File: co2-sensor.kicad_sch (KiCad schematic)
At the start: 51 parts, among them J1 Waveshare E-Ink, J2 USB-C Receptacle, J3 JST 2-PH, Q2 AO3400A, Q3 DMP2045U, SW1 SW_Push, SW2 SW_Push, SW3 SW_Push, SW4 SW_Push, SW5 SW_Push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

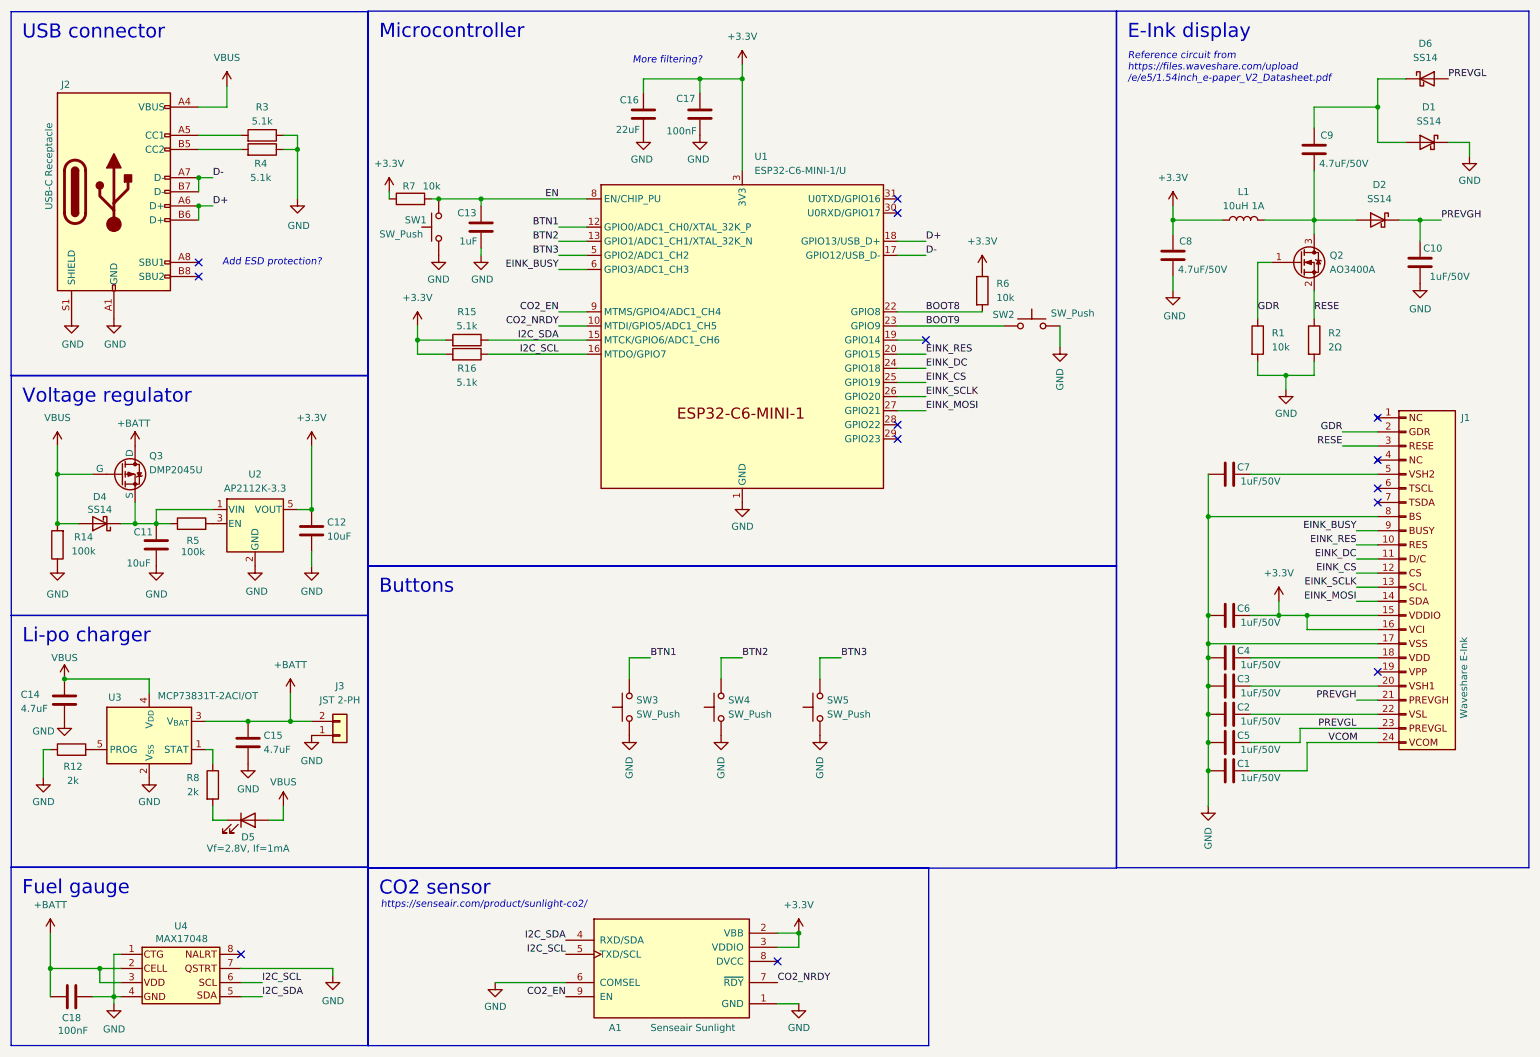
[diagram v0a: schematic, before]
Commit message: Add all LCSC part numbers
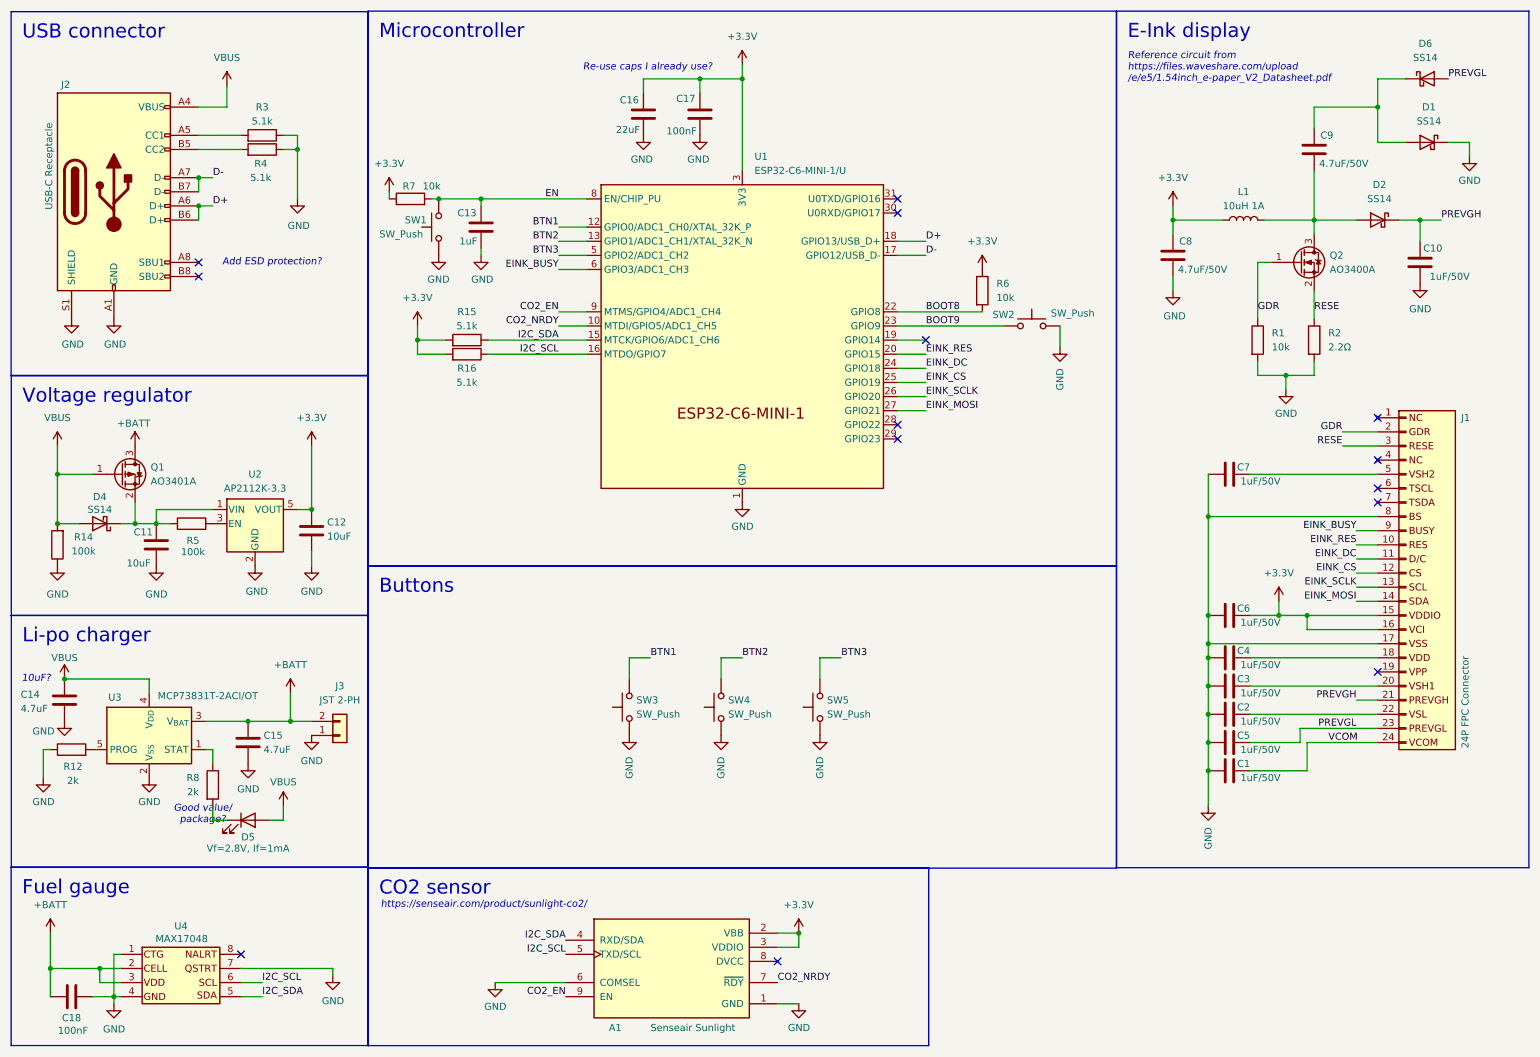
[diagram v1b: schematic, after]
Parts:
- removed Q3: DMP2045U, Package_TO_SOT_SMD:SOT-23, symbol Simulation_SPICE:PMOS
- added Q1: AO3401A, Package_TO_SOT_SMD:SOT-23, symbol Transistor_FET:AO3401A
- A1: now left out of the parts list
- C1, C10, C13, C2, C3, C4, C5, C6, C7: footprint Capacitor_SMD:C_0805_2012Metric -> Capacitor_SMD:C_0603_1608Metric; LCSC Part (none) -> C15849
- C11, C12: footprint Capacitor_SMD:C_0805_2012Metric -> Capacitor_SMD:C_0603_1608Metric; LCSC Part (none) -> C96446
- C14, C15, C8, C9: footprint Capacitor_SMD:C_0805_2012Metric -> Capacitor_SMD:C_1206_3216Metric; LCSC Part (none) -> C29823
- C16: LCSC Part (none) -> C45783
- C17, C18: LCSC Part (none) -> C1710
- D1, D2, D6: LCSC Part (none) -> C2480
- D4: footprint Diode_SMD:D_SOD-123 -> Diode_SMD:D_SMA; LCSC Part (none) -> C2480
- D5: LCSC Part (none) -> C2290
- J1: value Waveshare E-Ink -> 24P FPC Connector; footprint Connector_FFC-FPC:TE_2-1734839-4_1x24-1MP_P0.5mm_Horizontal -> Connector_FFC-FPC:Jushuo_AFC07-S24FCA-00_1x24-1MP_P0.50_Horizontal; LCSC Part (none) -> C262567
- J2: LCSC Part (none) -> C2988369
- J3: LCSC Part (none) -> C7433648
- L1: footprint Inductor_SMD:L_Ferrocore_DLG-0403 -> Inductor_SMD:L_1008_2520Metric; LCSC Part (none) -> C602018
- Q2: LCSC Part (none) -> C20917
- R1: LCSC Part (none) -> C25804
- R12, R8: footprint Capacitor_SMD:C_0805_2012Metric -> Resistor_SMD:R_0402_1005Metric; LCSC Part (none) -> C4109
- R14, R5: footprint Capacitor_SMD:C_0805_2012Metric -> Resistor_SMD:R_0402_1005Metric; LCSC Part (none) -> C25741
- R15, R16, R3, R4: footprint Capacitor_SMD:C_0805_2012Metric -> Resistor_SMD:R_0603_1608Metric; LCSC Part (none) -> C23186
- R2: value 2Ω -> 2.2Ω; LCSC Part (none) -> C22939
- R6, R7: footprint Capacitor_SMD:C_0805_2012Metric -> Resistor_SMD:R_0603_1608Metric; LCSC Part (none) -> C25804
- SW1, SW2, SW3, SW4, SW5: footprint Button_Switch_SMD:SW_SPST_SKQG_WithStem -> Button_Switch_SMD:SW_Push_1P1T_XKB_TS-1187A; LCSC Part (none) -> C318884
- U1: LCSC Part (none) -> C5736265
- U2: LCSC Part (none) -> C51118
- U3: LCSC Part (none) -> C424093
- U4: LCSC Part (none) -> C2682616
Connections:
- net +BATT: now also Q1.3 (D)
- net VBUS: now also Q1.1 (G)
- net at C11.1, D4.1 (K), R5.1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: now also Q1.2 (S)
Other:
- note added: "10uF?"
- note added: "Good value/ package?"
- note added: "Re-use caps I already use?"
- note removed: "More filtering?"

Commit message: Move components around
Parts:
- D1, D2, D4, D6: footprint Diode_SMD:D_SMA -> Diode_SMD:D_SOD-123; LCSC Part C2480 -> C8598
- J1: value 24P FPC Connector -> 24-pin FPC Connector; JLCPCB Position Offset (none) -> 0,0.381
- J2: JLCPCB Position Offset (none) -> 0,1.3335
- J3: JLCPCB Rotation Offset (none) -> 180
- U1: JLCPCB Position Offset (none) -> 0,-2.667
- U2, U3: JLCPCB Rotation Offset (none) -> 90
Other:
- note added: "Re-use caps sizes already use?"
- note removed: "10uF?"
- note removed: "Good value/ package?"
- note removed: "Re-use caps I already use?"
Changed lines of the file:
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@@
 	(title_block
 		(title "Low-Power CO2 Sensor")
-		(date "2024-11-01")
+		(date "2024-11-21")
 		(company "blinry <mail@blinry.org>")
 	)
@@
 		)
 	)
-	(text "Re-use caps I already use?"
+	(text "Re-use caps sizes already use?"
 		(exclude_from_sim no)
 		(at 126.492 22.098 0)
@@
 		)
 	)
-	(text "10uF?"
-		(exclude_from_sim no)
-		(at 16.51 132.08 0)
-		(effects
-			(font
-				(size 1.27 1.27)
-				(italic yes)
-				(color 255 0 0 1)
-			)
-		)
-	)
 	(text "Reference circuit from\nhttps://files.waveshare.com/upload\n/e/e5/1.54inch_e-paper_V2_Datasheet.pdf"
 		(exclude_from_sim no)
@@
 		)
 	)
-	(text "Good value/\npackage?"
-		(exclude_from_sim no)
-		(at 46.482 156.464 0)
-		(effects
-			(font
-				(size 1.27 1.27)
-				(italic yes)
-				(color 255 0 0 1)
-			)
-		)
-	)
 	(label "BTN2"
 		(at 143.51 128.27 0)
@@
 			)
 		)
-		(property "Footprint" "Diode_SMD:D_SMA"
+		(property "Footprint" "Diode_SMD:D_SOD-123"
 			(at 27.94 99.695 0)
 			(effects
@@
 			)
 		)
-		(property "LCSC Part" "C2480"
+		(property "LCSC Part" "C8598"
 			(at 27.94 104.14 0)
 			(effects
@@
 			)
 		)
+		(property "JLCPCB Position Offset" "0,-2.667"
+			(at 143.51 73.66 0)
+			(effects
+				(font
+					(size 1.27 1.27)
+				)
+				(hide yes)
+			)
+		)
 		(pin "46"
 		)
@@
 			)
 		)
+		(property "JLCPCB Rotation Offset" "180"
+			(at 71.12 142.24 0)
+			(effects
+				(font
+					(size 1.27 1.27)
+				)
+				(hide yes)
+			)
+		)
 		(pin "1"
 		)
@@
 			)
 		)
+		(property "JLCPCB Position Offset" "0,1.3335"
+			(at 30.48 44.45 0)
+			(effects
+				(font
+					(size 1.27 1.27)
+				)
+				(hide yes)
+			)
+		)
 		(pin "A1"
 		)
@@
 			)
 		)
-		(property "Value" "24P FPC Connector"
+		(property "Value" "24-pin FPC Connector"
 			(at 273.558 144.526 90)
 			(effects
@@
 			)
 		)
+		(property "JLCPCB Position Offset" "0,0.381"
+			(at 262.89 113.03 0)
+			(effects
+				(font
+					(size 1.27 1.27)
+				)
+				(hide yes)
+			)
+		)
 		(pin "17"
 		)
@@
 			)
 		)
+		(property "JLCPCB Rotation Offset" "90"
+			(at 55.88 104.14 0)
+			(effects
+				(font
+					(size 1.27 1.27)
+				)
+				(hide yes)
+			)
+		)
 		(pin "3"
 		)
@@
 			)
 		)
-		(property "Footprint" "Diode_SMD:D_SMA"
+		(property "Footprint" "Diode_SMD:D_SOD-123"
 			(at 266.7 40.005 0)
 			(effects
@@
 			)
 		)
-		(property "LCSC Part" "C2480"
+		(property "LCSC Part" "C8598"
 			(at 266.7 35.56 0)
 			(effects
@@
 			)
 		)
+		(property "JLCPCB Rotation Offset" "90"
+			(at 36.83 142.24 0)
+			(effects
+				(font
+					(size 1.27 1.27)
+				)
+				(hide yes)
+			)
+		)
 		(pin "2"
 		)
@@
 			)
 		)
-		(property "Footprint" "Diode_SMD:D_SMA"
+		(property "Footprint" "Diode_SMD:D_SOD-123"
 			(at 257.81 53.975 0)
 			(effects
@@
 			)
 		)
-		(property "LCSC Part" "C2480"
+		(property "LCSC Part" "C8598"
 			(at 257.81 49.53 0)
 			(effects
@@
 			)
 		)
-		(property "Footprint" "Diode_SMD:D_SMA"
+		(property "Footprint" "Diode_SMD:D_SOD-123"
 			(at 266.7 28.575 0)
 			(effects
@@
 			)
 		)
-		(property "LCSC Part" "C2480"
+		(property "LCSC Part" "C8598"
 			(at 266.7 24.13 0)
 			(effects

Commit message: Don't know?
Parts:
- removed D4: SS14, Diode_SMD:D_SOD-123, symbol Diode:MBR0540
- added D3: B5819W, Diode_SMD:D_SOD-123, symbol Diode:MBR0540
- D1, D2, D6: value SS14 -> B5819W
- J1: LCSC Part C262567 -> C262643
- SW1, SW2, SW3, SW4, SW5: footprint Button_Switch_SMD:SW_Push_1P1T_XKB_TS-1187A -> footprints:TS24CA
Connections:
- net VBUS: now also D3.2 (A)
- net at C11.1, Q1.2 (S), R5.1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: now also D3.1 (K)
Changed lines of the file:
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@@
 	(wire
 		(pts
-			(xy 24.13 104.14) (xy 20.32 104.14)
-		)
-		(stroke
-			(width 0)
-			(type default)
-		)
-	)
-	(wire
-		(pts
 			(xy 123.19 128.27) (xy 127 128.27)
 		)
@@
 	(wire
 		(pts
-			(xy 38.1 104.14) (xy 34.29 104.14)
-		)
-		(stroke
-			(width 0)
-			(type default)
-		)
-	)
-	(wire
-		(pts
 			(xy 57.15 186.69) (xy 53.34 186.69)
 		)
@@
 	(wire
 		(pts
-			(xy 34.29 104.14) (xy 31.75 104.14)
-		)
-		(stroke
-			(width 0)
-			(type default)
-		)
-	)
-	(wire
-		(pts
 			(xy 66.04 90.17) (xy 66.04 101.6)
 		)
@@
 	(wire
 		(pts
+			(xy 34.29 104.14) (xy 38.1 104.14)
+		)
+		(stroke
+			(width 0)
+			(type default)
+		)
+	)
+	(wire
+		(pts
 			(xy 50.8 25.4) (xy 50.8 29.21)
 		)
@@
 	(wire
 		(pts
+			(xy 31.75 104.14) (xy 34.29 104.14)
+		)
+		(stroke
+			(width 0)
+			(type default)
+		)
+	)
+	(wire
+		(pts
 			(xy 63.5 34.29) (xy 63.5 36.83)
 		)
@@
 	(wire
 		(pts
+			(xy 20.32 104.14) (xy 24.13 104.14)
+		)
+		(stroke
+			(width 0)
+			(type default)
+		)
+	)
+	(wire
+		(pts
 			(xy 227.33 125.73) (xy 257.81 125.73)
 		)
@@
 			)
 		)
-		(property "Footprint" "Button_Switch_SMD:SW_Push_1P1T_XKB_TS-1187A"
+		(property "Footprint" "footprints:TS24CA"
 			(at 195.58 63.5 0)
 			(effects
@@
 			)
 		)
-		(property "Footprint" "Button_Switch_SMD:SW_Push_1P1T_XKB_TS-1187A"
+		(property "Footprint" "footprints:TS24CA"
 			(at 118.11 137.16 0)
 			(effects
@@
 	)
 	(symbol
-		(lib_id "Diode:MBR0540")
-		(at 27.94 104.14 180)
-		(unit 1)
-		(exclude_from_sim no)
-		(in_bom yes)
-		(on_board yes)
-		(dnp no)
-		(property "Reference" "D4"
-			(at 27.94 99.314 0)
-			(effects
-				(font
-					(size 1.27 1.27)
-				)
-			)
-		)
-		(property "Value" "SS14"
-			(at 27.94 101.6 0)
-			(effects
-				(font
-					(size 1.27 1.27)
-				)
-			)
-		)
-		(property "Footprint" "Diode_SMD:D_SOD-123"
-			(at 27.94 99.695 0)
-			(effects
-				(font
-					(size 1.27 1.27)
-				)
-				(hide yes)
-			)
-		)
-		(property "Datasheet" "https://www.vishay.com/docs/88746/ss12.pdf"
-			(at 27.94 104.14 0)
-			(effects
-				(font
-					(size 1.27 1.27)
-				)
-				(hide yes)
-			)
-		)
-		(property "Description" "40V 0.5A Schottky Power Rectifier Diode, SOD-123"
-			(at 27.94 104.14 0)
-			(effects
-				(font
-					(size 1.27 1.27)
-				)
-				(hide yes)
-			)
-		)
-		(property "LCSC Part" "C8598"
-			(at 27.94 104.14 0)
-			(effects
-				(font
-					(size 1.27 1.27)
-				)
-				(hide yes)
-			)
-		)
-		(property "Sim.Device" ""
-			(at 27.94 104.14 0)
-			(effects
-				(font
-					(size 1.27 1.27)
-				)
-				(hide yes)
-			)
-		)
-		(property "Sim.Pins" ""
-			(at 27.94 104.14 0)
-			(effects
-				(font
-					(size 1.27 1.27)
-				)
-				(hide yes)
-			)
-		)
-		(property "Sim.Type" ""
-			(at 27.94 104.14 0)
-			(effects
-				(font
-					(size 1.27 1.27)
-				)
-				(hide yes)
-			)
-		)
-		(pin "2"
-		)
-		(pin "1"
-		)
-		(instances
-			(project ""
-				(path "/14a75f0f-668c-4fbd-ad64-ed80bbf70e47"
-					(reference "D4")
-					(unit 1)
-				)
-			)
-		)
-	)
-	(symbol
 		(lib_id "power:GND")
 		(at 66.04 142.24 0)
@@
 			)
 		)
-		(property "Footprint" "Button_Switch_SMD:SW_Push_1P1T_XKB_TS-1187A"
+		(property "Footprint" "footprints:TS24CA"
 			(at 152.4 137.16 0)
 			(effects
@@
 	)
 	(symbol
+		(lib_id "Diode:MBR0540")
+		(at 27.94 104.14 180)
+		(unit 1)
+		(exclude_from_sim no)
+		(in_bom yes)
+		(on_board yes)
+		(dnp no)
+		(property "Reference" "D3"
+			(at 27.94 98.806 0)
+			(effects
+				(font
+					(size 1.27 1.27)
+				)
+			)
+		)
+		(property "Value" "B5819W"
+			(at 27.94 101.092 0)
+			(effects
+				(font
+					(size 1.27 1.27)
+				)
+			)
+		)
+		(property "Footprint" "Diode_SMD:D_SOD-123"
+			(at 27.94 99.695 0)
+			(effects
+				(font
+					(size 1.27 1.27)
+				)
+				(hide yes)
+			)
+		)
+		(property "Datasheet" "~"
+			(at 27.94 104.14 0)
+			(effects
+				(font
+					(size 1.27 1.27)
+				)
+				(hide yes)
+			)
+		)
+		(property "Description" "40V 0.5A Schottky Power Rectifier Diode, SOD-123"
+			(at 27.94 104.14 0)
+			(effects
+				(font
+					(size 1.27 1.27)
+				)
+				(hide yes)
+			)
+		)
+		(property "LCSC Part" "C8598"
+			(at 27.94 104.14 0)
+			(effects
+				(font
+					(size 1.27 1.27)
+				)
+				(hide yes)
+			)
+		)
+		(property "Sim.Device" ""
+			(at 27.94 104.14 0)
+			(effects
+				(font
+					(size 1.27 1.27)
+				)
+				(hide yes)
+			)
+		)
+		(property "Sim.Pins" ""
+			(at 27.94 104.14 0)
+			(effects
+				(font
+					(size 1.27 1.27)
+				)
+				(hide yes)
+			)
+		)
+		(property "Sim.Type" ""
+			(at 27.94 104.14 0)
+			(effects
+				(font
+					(size 1.27 1.27)
+				)
+				(hide yes)
+			)
+		)
+		(pin "2"
+		)
+		(pin "1"
+		)
+		(instances
+			(project "co2-sensor"
+				(path "/14a75f0f-668c-4fbd-ad64-ed80bbf70e47"
+					(reference "D3")
+					(unit 1)
+				)
+			)
+		)
+	)
+	(symbol
 		(lib_id "power:GND")
 		(at 96.52 55.88 0)
@@
 			)
 		)
-		(property "LCSC Part" "C262567"
+		(property "LCSC Part" "C262643"
 			(at 262.89 113.03 0)
 			(effects
@@
 			)
 		)
-		(property "Value" "SS14"
+		(property "Value" "B5819W"
 			(at 267.0175 31.75 0)
 			(effects
@@
 			)
 		)
-		(property "Datasheet" "https://www.vishay.com/docs/88746/ss12.pdf"
+		(property "Datasheet" "~"
 			(at 266.7 35.56 0)
 			(effects
@@
 			)
 		)
-		(property "Value" "SS14"
+		(property "Value" "B5819W"
 			(at 258.1275 45.72 0)
 			(effects
@@
 			)
 		)
-		(property "Datasheet" "https://www.vishay.com/docs/88746/ss12.pdf"
+		(property "Datasheet" "~"
 			(at 257.81 49.53 0)
 			(effects
@@
 			)
 		)
-		(property "Footprint" "Button_Switch_SMD:SW_Push_1P1T_XKB_TS-1187A"
+		(property "Footprint" "footprints:TS24CA"
 			(at 134.62 137.16 0)
 			(effects
@@
 			)
 		)
-		(property "Footprint" "Button_Switch_SMD:SW_Push_1P1T_XKB_TS-1187A"
+		(property "Footprint" "footprints:TS24CA"
 			(at 83.82 50.8 0)
 			(effects
@@
 			)
 		)
-		(property "Value" "SS14"
+		(property "Value" "B5819W"
 			(at 266.3825 20.32 0)
 			(effects
@@
 			)
 		)
-		(property "Datasheet" "https://www.vishay.com/docs/88746/ss12.pdf"
+		(property "Datasheet" "~"
 			(at 266.7 24.13 0)
 			(effects
